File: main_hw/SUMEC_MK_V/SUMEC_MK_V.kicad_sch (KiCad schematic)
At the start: 10 parts

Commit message: 67yfhtgftu
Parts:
- renumbered TP19 to TP1, TP22 to TP10, TP1 to TP2, TP2 to TP3, TP3 to TP4, TP4 to TP5, TP5 to TP6, TP6 to TP7, TP20 to TP8, TP21 to TP9
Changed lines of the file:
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@@
 		(dnp no)
 		(fields_autoplaced yes)
-		(property "Reference" "TP20"
+		(property "Reference" "TP8"
 			(at 165.1 184.6579 0)
 			(effects
@@
 			(project "SUMEC_MK_V"
 				(path "/900bd7ac-cdf9-4a2f-8b1f-2c21e3760046"
-					(reference "TP20")
+					(reference "TP8")
 					(unit 1)
 				)
@@
 		(dnp no)
 		(fields_autoplaced yes)
-		(property "Reference" "TP4"
+		(property "Reference" "TP5"
 			(at 153.67 184.6579 0)
 			(effects
@@
 			(project "SUMEC_MK_V"
 				(path "/900bd7ac-cdf9-4a2f-8b1f-2c21e3760046"
-					(reference "TP4")
+					(reference "TP5")
 					(unit 1)
 				)
@@
 		(dnp no)
 		(fields_autoplaced yes)
-		(property "Reference" "TP3"
+		(property "Reference" "TP4"
 			(at 149.86 184.6579 0)
 			(effects
@@
 			(project "SUMEC_MK_V"
 				(path "/900bd7ac-cdf9-4a2f-8b1f-2c21e3760046"
-					(reference "TP3")
+					(reference "TP4")
 					(unit 1)
 				)
@@
 		(dnp no)
 		(fields_autoplaced yes)
-		(property "Reference" "TP22"
+		(property "Reference" "TP10"
 			(at 172.72 184.6579 0)
 			(effects
@@
 			(project "SUMEC_MK_V"
 				(path "/900bd7ac-cdf9-4a2f-8b1f-2c21e3760046"
-					(reference "TP22")
+					(reference "TP10")
 					(unit 1)
 				)
@@
 		(dnp no)
 		(fields_autoplaced yes)
-		(property "Reference" "TP21"
+		(property "Reference" "TP9"
 			(at 168.91 184.6579 0)
 			(effects
@@
 			(project "SUMEC_MK_V"
 				(path "/900bd7ac-cdf9-4a2f-8b1f-2c21e3760046"
-					(reference "TP21")
+					(reference "TP9")
 					(unit 1)
 				)
@@
 		(dnp no)
 		(fields_autoplaced yes)
-		(property "Reference" "TP5"
+		(property "Reference" "TP6"
 			(at 157.48 184.6579 0)
 			(effects
@@
 			(project "SUMEC_MK_V"
 				(path "/900bd7ac-cdf9-4a2f-8b1f-2c21e3760046"
-					(reference "TP5")
+					(reference "TP6")
 					(unit 1)
 				)
@@
 		(dnp no)
 		(fields_autoplaced yes)
-		(property "Reference" "TP6"
+		(property "Reference" "TP7"
 			(at 161.29 184.6579 0)
 			(effects
@@
 			(project "SUMEC_MK_V"
 				(path "/900bd7ac-cdf9-4a2f-8b1f-2c21e3760046"
-					(reference "TP6")
+					(reference "TP7")
 					(unit 1)
 				)
@@
 		(dnp no)
 		(fields_autoplaced yes)
-		(property "Reference" "TP19"
+		(property "Reference" "TP1"
 			(at 138.43 184.6579 0)
 			(effects
@@
 			(project "SUMEC_MK_V"
 				(path "/900bd7ac-cdf9-4a2f-8b1f-2c21e3760046"
-					(reference "TP19")
+					(reference "TP1")
 					(unit 1)
 				)
@@
 		(dnp no)
 		(fields_autoplaced yes)
-		(property "Reference" "TP1"
+		(property "Reference" "TP2"
 			(at 142.24 184.6579 0)
 			(effects
@@
 			(project "SUMEC_MK_V"
 				(path "/900bd7ac-cdf9-4a2f-8b1f-2c21e3760046"
-					(reference "TP1")
+					(reference "TP2")
 					(unit 1)
 				)
@@
 		(dnp no)
 		(fields_autoplaced yes)
-		(property "Reference" "TP2"
+		(property "Reference" "TP3"
 			(at 146.05 184.6579 0)
 			(effects
@@
 			(project "SUMEC_MK_V"
 				(path "/900bd7ac-cdf9-4a2f-8b1f-2c21e3760046"
-					(reference "TP2")
-					(unit 1)
-				)
+					(reference "TP3")
+					(unit 1)
+				)

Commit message: MK5 changes and deletion of useless files
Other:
- note added: "1. Q: Fix EEPROM 2. Q: I2C expander for more LEDs 3. Q: Power switching for higher voltage (if the battery is connested choose the battery) 4. Q: Fix errors in schematic encoders etc 5. Q: 6. Q: 7. Q:"
- note removed: "*The unit price is set for an order quantity of 10 units"
- note removed: "1. Q: 2. Q: 3. Q: Left/right silk for sensors and motors 4. Q: 5. Q: Add IO pin numbers after the routing is done 6. Q: Does the voltage read need to be after the switch or before? 7. Q:"
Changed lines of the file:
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@@
 		)
 	)
-	(text "1. Q: \n2. Q: \n3. Q: Left/right silk for sensors and motors\n4. Q: \n5. Q: Add IO pin numbers after the routing is done\n6. Q: Does the voltage read need to be after the switch or before?\n7. Q: "
+	(text "1. Q: Fix EEPROM\n2. Q: I2C expander for more LEDs\n3. Q: Power switching for higher voltage \n	(if the battery is connested choose the battery)\n4. Q: Fix errors in schematic encoders etc\n5. Q: \n6. Q: \n7. Q: "
 		(exclude_from_sim no)
 		(at 20.32 183.134 0)
@@
 		)
 	)
-	(text "*The unit price is set for an order quantity of 10 units"
-		(exclude_from_sim no)
-		(at 52.07 173.99 0)
-		(effects
-			(font
-				(face "Bahnschrift")
-				(size 1.905 1.905)
-				(color 255 0 0 1)
-			)
-		)
-	)

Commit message: MK5 PCB rework
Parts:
- removed TP1: TestPoint, sumec_graphic:SUMEC_QR_IMG, symbol Connector:TestPoint
- removed TP10: TestPoint, sumec_graphic:SYMBOL_IMG, symbol Connector:TestPoint
- removed TP2: TestPoint, sumec_graphic:SPS_LOGO_IMG, symbol Connector:TestPoint
- removed TP3: TestPoint, sumec_graphic:SUMEC_LOGO_IMG, symbol Connector:TestPoint
- removed TP4: TestPoint, sumec_graphic:CATTO_MASK_IMG, symbol Connector:TestPoint
- removed TP5: TestPoint, sumec_graphic:OWO_WHATS_THIS_IMG, symbol Connector:TestPoint
- removed TP6: TestPoint, sumec_graphic:HANKA_THINGY_IMG, symbol Connector:TestPoint
- removed TP7: TestPoint, sumec_graphic:CALIPER_IMG, symbol Connector:TestPoint
- removed TP8: TestPoint, sumec_graphic:BEE_IMG, symbol Connector:TestPoint
- removed TP9: TestPoint, sumec_graphic:FLOWER_IMG, symbol Connector:TestPoint
- added BZ1: Buzzer, Schrack_brd:BUZZER_CUI_CPT, symbol Device:Buzzer
- added C1, C11, C16, C17, C20, C22, C23, C24, C25, C26, C4: 100nF, Capacitor_SMD:C_0805_2012Metric_Pad1.18x1.45mm_HandSolder, symbol Device:C
- added C10, C3, C6, C7, C8, C9: 22uF, Capacitor_Tantalum_SMD:CP_EIA-2012-12_Kemet-R_Pad1.30x1.05mm_HandSolder, symbol Device:C_Polarized
- added C12, C14: 22nF, Capacitor_SMD:C_0805_2012Metric_Pad1.18x1.45mm_HandSolder, symbol Device:C_Small
- added C13, C15, C5: 100nF, Capacitor_SMD:C_0805_2012Metric_Pad1.18x1.45mm_HandSolder, symbol Device:C_Small
- added C18, C19, C2, C21: 10uF, Capacitor_Tantalum_SMD:CP_EIA-3216-18_Kemet-A_Pad1.58x1.35mm_HandSolder, symbol Device:C_Polarized
- added C27, C29: 10uF, Capacitor_Tantalum_SMD:CP_EIA-3216-18_Kemet-A_Pad1.58x1.35mm_HandSolder, symbol Device:C_Polarized_Small
- added C28, C33, C34, C35, C36, C37: 100n, Capacitor_SMD:C_0805_2012Metric, symbol Device:C_Small
- added C30: 1u, Capacitor_SMD:C_0805_2012Metric, symbol Device:C_Small
- added C31, C32: 18p, Capacitor_SMD:C_0805_2012Metric, symbol Device:C_Small
- added D1, D2: D_Schottky, Diode_SMD:D_1206_3216Metric_Pad1.42x1.75mm_HandSolder, symbol Device:D_Schottky
- added D10: ALRT2, LED_SMD:LED_0805_2012Metric, symbol Device:LED_Small
- added D11, D12: D_Schottky, Diode_SMD:D_1206_3216Metric, symbol Device:D_Schottky
- added D3: D, symbol Device:D
- added D4, D5, D6, D7, D8, D9: LED, LED_SMD:LED_0805_2012Metric_Pad1.15x1.40mm_HandSolder, symbol Device:LED
- added H1, H2: Mounting Hole M3, MountingHole:MountingHole_3.2mm_M3_Pad_Via, symbol Mechanical:MountingHole_Pad
- added IC1: TPS565242DRLR, Package_TO_SOT_SMD:SOT-563, symbol SamacSys_Parts:TPS565242DRLR
- added IC2, IC3: DRV8874PWPR, sumec_brd:DRV8874, symbol sumec_sch_lib:DRV8874PWPR
- added J1: XT30PW-M, sumec_brd:XT30PW-M, symbol sumec_sch_lib:XT30PW-M
- added J10, J12, J13, J7, J8, J9: Conn_01x03_Pin, Connector_Molex:Molex_PicoBlade_53398-0371_1x03-1MP_P1.25mm_Vertical, symbol Connector:Conn_01x03_Pin
- added J11: Conn_01x03_Pin, Connector_PinHeader_2.54mm:PinHeader_1x03_P2.54mm_Vertical, symbol Connector:Conn_01x03_Pin
- added J14, J15, J4: USB_TypeC, sumec_brd:HRO_TYPE-C-31-M-12, symbol sumec_sch_lib:USB_TypeC
- added J2, J3: Conn_01x06_Socket, Connector_JST:JST_SH_BM06B-SRSS-TB_1x06-1MP_P1.00mm_Vertical, symbol Connector:Conn_01x06_Socket
- added J5: Conn_01x04_Pin, Connector_Molex:Molex_PicoBlade_53398-0471_1x04-1MP_P1.25mm_Vertical, symbol Connector:Conn_01x04_Pin
- added J6: Conn_01x06_Pin, Connector_Molex:Molex_PicoBlade_53398-0671_1x06-1MP_P1.25mm_Vertical, symbol Connector:Conn_01x06_Pin
- added JP1, JP2, JP3: SolderJumper_3_Open, Jumper:SolderJumper-3_P2.0mm_Open_TrianglePad1.0x1.5mm, symbol Jumper:SolderJumper_3_Open
- added JP4, JP5, JP6: Jumper_2_Small_Open, Jumper:SolderJumper-2_P1.3mm_Open_RoundedPad1.0x1.5mm, symbol Jumper:Jumper_2_Small_Open
- added L1: 1.5uH, Inductor_SMD:L_Vishay_IHLP-1212, symbol Device:L
- added L2: 3.3uH, Inductor_SMD:L_Vishay_IHLP-1616, symbol Device:L
- added Q1: Q_PMOS, Package_TO_SOT_SMD:SOT-23-3, symbol Device:Q_PMOS_GSD
- added Q2: SI2393DS, Package_TO_SOT_SMD:SOT-23-3, symbol Device:Q_PMOS_GSD
- added R1: 2m, Resistor_SMD:R_0805_2012Metric_Pad1.20x1.40mm_HandSolder, symbol Device:R
- added R10, R25, R26, R9: 10k, Resistor_SMD:R_0805_2012Metric_Pad1.20x1.40mm_HandSolder, symbol Device:R_Small
- added R11, R12, R2, R23, R24, R27, R3, R7: 10k, Resistor_SMD:R_0805_2012Metric_Pad1.20x1.40mm_HandSolder, symbol Device:R
- added R13: 1k, Resistor_SMD:R_0805_2012Metric_Pad1.20x1.40mm_HandSolder, symbol Device:R
- added R14, R16, R17, R20, R21: 220R, Resistor_SMD:R_0805_2012Metric_Pad1.20x1.40mm_HandSolder, symbol Device:R
- added R15: 100k, Resistor_SMD:R_0805_2012Metric_Pad1.20x1.40mm_HandSolder, symbol Device:R
- added R18, R19: 15R, Resistor_SMD:R_0805_2012Metric_Pad1.20x1.40mm_HandSolder, symbol Device:R
- added R22: 0R, Resistor_SMD:R_0805_2012Metric_Pad1.20x1.40mm_HandSolder, symbol Device:R
- added R28: 100R, Resistor_SMD:R_0805_2012Metric_Pad1.20x1.40mm_HandSolder, symbol Device:R
- added R29, R30, R31, R32, R33, R38: 10k, Resistor_SMD:R_0805_2012Metric, symbol Device:R_Small
- added R34, R40: 100k, Resistor_SMD:R_0805_2012Metric, symbol Device:R_Small
- added R35, R36: 15R, Resistor_SMD:R_0805_2012Metric, symbol Device:R
- added R37: 50m, Resistor_SMD:R_0805_2012Metric, symbol Device:R
- added R39: 2.2k, Resistor_SMD:R_0805_2012Metric, symbol Device:R_Small
- added R4: 45k, Resistor_SMD:R_0805_2012Metric_Pad1.20x1.40mm_HandSolder, symbol Device:R
- added R41, R42: 5.1k, Resistor_SMD:R_0805_2012Metric, symbol Device:R_Small
- added R43, R44: 15R, Resistor_SMD:R_0805_2012Metric, symbol Device:R_Small
- added R45: 10k, Resistor_SMD:R_0805_2012Metric, symbol Device:R
- added R5: 100k, Resistor_SMD:R_0805_2012Metric_Pad1.20x1.40mm_HandSolder, symbol Device:R_Small
- added R6, R8: 52.3k, Resistor_SMD:R_0805_2012Metric_Pad1.20x1.40mm_HandSolder, symbol Device:R_Small
- added SW1: SW_DPDT_x2, sumec_brd:Custom_SPDT_2.5_Switch, symbol Switch:SW_DPDT_x2
- added SW2, SW3, SW4, SW5: SW_Push, sumec_brd:SW_SPST_EVQPE1, symbol Switch:SW_Push
- added SW6: RST, gps-compass_brd:SW_SPST_EVQPE1, symbol Switch:SW_Push
- added TP11, TP12, TP13, TP14, TP15, TP16, TP17, TP18, TP19, TP20, TP21, TP22, TP23, TP24, TP25: TestPoint, TestPoint:TestPoint_Pad_D1.0mm, symbol Connector:TestPoint
- added U1, U8: INA226, Package_SO:VSSOP-10_3x3mm_P0.5mm, symbol Sensor_Energy:INA226
- added U2: AP62300Z6, Package_TO_SOT_SMD:SOT-563, symbol Regulator_Switching:AP62300Z6
- added U3: 24CW1280T-I/OT, Package_TO_SOT_SMD:SOT-23-5, symbol Memory_EEPROM:24AA02-OT
- added U4: ESP32-S3-WROOM-1, PCM_Espressif:ESP32-S3-WROOM-1, symbol sumec_sch_lib:ESP32-S3-WROOM-1_CUSTOM_made_by_bismarx
- added U5, U7, U9: USBLC6-2SC6, Package_TO_SOT_SMD:TSOT-23-6_HandSoldering, symbol sumec_library:USBLC6-2SC6
- added U6: BNO055, Package_LGA:LGA-28_5.2x3.8mm_P0.5mm, symbol Sensor_Motion:BNO055
- added Y1: 32.768k, gps-compass_brd:CM8V32768TA020125, symbol Device:Crystal
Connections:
- new net: D9.2 (A), R21.2
- new net: R5.2, R6.1, U2.5 (EN)
- new net: C15.1, IC3.12 (VCP)
- new net: D8.2 (A), R20.2
- new net: C33.1, J14.S1 (SHIELD), J14.S2 (SHIELD), J14.S3 (SHIELD), J14.S4 (SHIELD), R34.1
- new net: D4.2 (A), R13.2
- new net: C12.1, IC2.14 (CPL)
- new net: C12.2, IC2.13 (CPH)
- new net: D5.2 (A), R14.2
- new net: C32.1, U6.27 (XIN32), Y1.1
- new net: C31.1, U6.26 (XOUT32), Y1.2
- new net: JP5.1 (A), R32.2, U6.6 (PS0)
- new net: R30.1, SW6.2, U6.11 (~{RESET})
- new net: JP4.1 (A), R31.2, U6.17 (COM3)
- new net: R29.1, TP25.1, U6.4 (~{BOOT_LOAD_PIN})
- new net: JP6.1 (A), R33.2, U6.5 (PS1)
- new net: C30.1, U6.9 (CAP)
- new net: R43.2, U9.1
- new net: R44.2, U9.3
- new net: D10.1 (K), R38.2, U8.3 (~{Alert})
- new net: C34.1, U7.5
- new net: C13.1, IC2.12 (VCP)
- new net: D6.2 (A), R16.2
- new net: J15.A5 (CC1), R42.1
- new net: J15.B5 (CC2), R41.2
- new net: C36.2, J15.S1 (SHIELD), J15.S2 (SHIELD), J15.S3 (SHIELD), J15.S4 (SHIELD), R40.2
- new net: R18.2, U5.1
- new net: D10.2 (A), R39.2
- new net: R19.2, U5.3
- new net: C14.2, IC3.13 (CPH)
- new net: C14.1, IC3.14 (CPL)
- new net: C5.2, U2.4 (BST)
- new net: J7.2 (Pin_2), R28.2
- new net: D11.2 (A), Q2.3 (D)
- new net: IC1.2 (SW), L1.1
- new net: R36.2, U7.3
- new net: BZ1.1 (+), R22.2
- new net: R35.2, U7.1
- new net: D7.2 (A), R17.2
- new net +12V: C13.2, C15.2, C16.2, C17.2, C18.1, C19.1, C2.1, IC2.11 (VM), IC3.11 (VM), Q1.3 (D), R13.1, R5.1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
- new net +3V3: C1.2, C11.1, C20.1, C21.1, C22.1, C27.1, C28.1, C29.1, C35.1, C6.1, C7.1, C9.1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
- new net +5V: C3.1, C4.1, D1.1 (K), D3.1 (K), IC1.1 (VIN), IC1.5 (EN), J6.1 (Pin_1), TP12.1
- new net ACC_INT: U4.32 (IO39)
- new net BOOT: C26.1, R24.1, SW3.2, U4.27 (IO0)
- new net BTN_IO04: R25.2, SW4.2, U4.4 (IO4)
- new net BTN_IO05: R26.2, SW5.2, U4.5 (IO5)
- new net BZ_IO02: R22.1, U4.38 (IO2)
- new net CC1: J14.A5 (CC1)
- new net CC2: J14.B5 (CC2)
- new net D+: U4.14 (IO20), U5.4, U7.4, U9.6
- new net D-: U4.13 (IO19), U5.6, U7.6, U9.4
- new net DN_IN: J14.A7 (DN1), J14.B7 (DN2), J15.A7 (DN1), J15.B7 (DN2), R35.1, R44.1
- new net DP_IN: J14.A6 (DP1), J14.B6 (DP2), J15.A6 (DP1), J15.B6 (DP2), R36.1, R43.1
- new net D_NEG_IN: J4.A7 (DN1), J4.B7 (DN2), R18.1
- new net D_POS_IN: J4.A6 (DP1), J4.B6 (DP2), R19.1
- new net EN: C25.1, R23.1, SW2.2, U4.3 (EN)
- new net EN_L: IC2.1 (EN/IN1), TP15.1, U4.7 (IO7)
- new net EN_R: IC3.1 (EN/IN1), TP18.1, U4.12 (IO8)
- new net FB: IC1.6 (FB), R4.2, R7.1
- new net FB_5V: R8.2, R9.1, U2.6 (FB)
- new net FET_SW: Q1.1 (G), R2.2, SW1.1 (A)
- new net GND: BZ1.2 (-), C1.1, C10.2, C11.2, C16.1, C17.1, C18.2, C19.2, C2.2, C20.2, C21.2, C22.2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
- new net GYR_INT: U4.33 (IO40)
- new net INT_IMU: U6.14 (INT)
- new net IN_NEG_2: R37.2, U8.8 (Vbus), U8.9 (Vin-)
- new net IR_MODULE: J11.1 (Pin_1), TP19.1, U4.30 (IO37)
- new net LED_IO01: R21.1, U4.39 (IO1)
- new net LED_IO36: R20.1, U4.29 (IO36)
- new net LED_IO43: U4.37 (IO43)
- new net LED_IO44: R16.1, U4.36 (IO44)
- new net LED_IO47: R17.1
- new net MOTOR_L_1: IC2.8 (OUT1), J2.6 (Pin_6), TP23.1
- new net MOTOR_L_2: IC2.10 (OUT2), J2.5 (Pin_5), TP24.1
- new net MOTOR_R_1: IC3.8 (OUT1), J3.6 (Pin_6), TP21.1
- new net MOTOR_R_2: IC3.10 (OUT2), J3.5 (Pin_5), TP22.1
- new net OUT_L_A: J2.3 (Pin_3)
- new net OUT_L_B: J2.2 (Pin_2)
- new net OUT_R_A: J3.3 (Pin_3)
- new net OUT_R_B: J3.2 (Pin_2)
- new net PH_L: IC2.2 (PH/IN2), TP17.1, U4.6 (IO6)
- new net PH_R: IC3.2 (PH/IN2), TP20.1, U4.11 (IO18)
- new net PMODE_1: IC2.16 (PMODE), JP2.2 (C)
- new net PMODE_2: IC3.16 (PMODE), JP3.2 (C)
- new net POL_L: J10.1 (Pin_1), U4.28 (IO35)
- new net POL_M: J9.1 (Pin_1), U4.19 (IO11)
- new net POL_R: J8.1 (Pin_1), U4.20 (IO12)
- new net QRE_BACK: J7.1 (Pin_1), R27.2, U4.9 (IO16)
- new net QRE_L: J5.4 (Pin_4), U4.22 (IO14)
- new net QRE_R: J5.1 (Pin_1), U4.21 (IO13)
- new net SCL: J6.3 (Pin_3), R12.1, U1.5 (SCL), U3.1 (SCL), U4.34 (IO41), U6.19 (COM1), U8.5 (SCL)
- new net SDA: J6.2 (Pin_2), R11.1, U1.4 (SDA), U3.3 (SDA), U4.35 (IO42), U6.20 (COM0), U8.4 (SDA)
- new net SHARP_L: J13.1 (Pin_1), U4.31 (IO38)
- new net SHARP_R: J12.1 (Pin_1), U4.18 (IO10)
- new net SHLD: C23.2, J4.S1 (SHIELD), J4.S2 (SHIELD), J4.S3 (SHIELD), J4.S4 (SHIELD), R15.1
- new net SW: C5.1, L2.1, U2.2 (SW)
- new net USB_VBUS: C24.1, C37.2, D12.2 (A), J14.A4_B9 (VBUS), J14.B4_A9 (VBUS), J15.A4_B9 (VBUS), J15.B4_A9 (VBUS), J4.A4_B9 (VBUS), J4.B4_A9 (VBUS), Q2.1 (G), R45.1, U5.5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
- new net VBATT: J1.P, JP1.3 (B), R1.1, U1.10 (Vin+)
- new net VBATT_SHUNT: JP1.1 (A), Q1.2 (S), R1.2, R2.1, U1.9 (Vin-)
- new net VBATT_SW: Q2.2 (S)
- new net VBUS_INA226: JP1.2 (C), U1.8 (Vbus)
- new net VBUS_USB: D3.2 (A), R14.1, TP13.1
- new net VIN: D11.1 (K), D12.1 (K)
- new net VOLTAGE_ALERT: R3.2, U1.3 (~{Alert}), U4.17 (IO9)
- new net VOUT_5V: C10.1, C8.1, D1.2 (A), L2.2, R8.1
- new net nFAULT: IC2.4 (NFAULT), IC3.4 (NFAULT), R10.1, TP11.1
- no-connect marks 0 -> 16
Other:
- removed sheet CONNECTIVITY
- removed sheet MCU
- removed sheet MECHANICS
- removed sheet MOTOR CONTROL
- removed sheet POWER
- removed sheet SENSORICS
- note added: "( Better manual in -DOCS- )"
- note added: "- 2S/3S LiPo - 3.7V Cell voltage (nominal voltage) - 4,2V Cell voltage (fully charged) - 400mAh (may vary)"
- note added: "1. 2. 3. 4. 5. 6. 7."
- note added: "6-PIN JST SH-Style male connector VCC 2.7 V to 18 V encoder operating voltage"
- note added: "9-AXIS IMU"
- note added: "AP62301Z6-7 Step down converter Input: 4.2-18V Output: 5V Current output: 3A Switching freq.: 750kHz Inductor Inductance: 3.3uH Max. current: 2.7A"
- note added: "BAD PINOUT"
- note added: "BATTERY"
- note added: "BNO055 9 DOF Absolute IMU with intergrated sensor fusion"
- note added: "BOOT"
- note added: "BUZZER"
- note added: "Battery power"
- note added: "Buttons for BOOT and ENABLE functions. If the device does not support the auto download mode, you need to get into the download mode manually. To do so, press and hold the BOOT button and then press the RESET button once. After that release the BOOT button."
- note added: "CONNECTORS and MISC"
- note added: "CONTROL MODES: PMODE HIGH = PWM PMODE LOW = PH/EN"
- note added: "CURRENT READING - 2"
- note added: "DEBUG and MECHANICS"
- note added: "DISTANCE MEASURING"
- note added: "DRV8874 - Motor driver, H-Bridge Recommended Operating Conditions VM = 4.5V - 37V VM VIN = 0V - 5v I/PMODE, nSlEEP, EN/IN1, PH/IN2 fPWM = 0Hz - 100kHz EN/IN1, PH/IN2 Vref = 0V - 3.6V VREF Block Diagram:"
- note added: "Default Configuration of Strapping Pins Strapping Pin Default Configuration Bit Value GPIO0 Pull-up 1 GPIO3 Floating - GPIO45 Pull-down 0 GPIO46 Pull-down 0"
- note added: "Digital distance sensor - Sharp GP2Y0D810Z0F Sensor detects objects between 2 cm and 10 cm Low when detecting an object, high otherwise. Operating voltage 2.7V - 6.2V"
- note added: "EEPROM"
- note added: "EN-IN1"
- note added: "EN=reset, BOOT=bootloader mode Enable (EN) is the 3.3V regulator's enable pin. It's pulled up, so connect to ground to disable the 3.3V regulator. This means that you can use this pin connected to a pushbutton to restart your ESP32, for example."
- note added: "ENABLE RESET"
- note added: "ESD PROTECTION"
- note added: "ESP32-S3 Datasheet"
- note added: "ESP32-S3-WROOM1-N4"
- note added: "GPIO USB 20 D+ (green) 19 D- (white) GND GND (black) VBUS +5V (red)"
- note added: "GPIO0 has an internal pullup resistor, so if it is left unconnected then it will pull high."
- note added: "GPIO0, GPIO45, and GPIO46 are connected to the chip's internal weak pull-up/pull-down resistors at chip reset. These resistors determine the default bit values of the strapping pins. Also, these resistors determine the bit values if the strapping pins are connected to an external high-impedance circuit."
- note added: "H-BRIDGE"
- note added: "I2C Addr.: 0x28"
- note added: "I2C Addr.: 0x50"
- note added: "I2C adress = 0x40"
- note added: "I2C adress = 0x44, 1000100"
- note added: "IR LED Reciver module Operating voltage: 2.7V to 5.5V Frequency: 38kHz"
- note added: "IR MODULE"
- note added: "ITRIP (A) x AIPROPI (μA/A) = VVREF (V) / RIPROPI (Ω)"
- note added: "LED SIGNALISATION"
- note added: "LEFT"
- note added: "LINE SENSORS"
- note added: "M3 Padded Mounting holes"
- note added: "MAIN SWITCH"
- note added: "MCU and IMU"
- note added: "MIRRORED"
- note added: "MOTOR - LEFT"
- note added: "MOTOR - RIGHT"
- note added: "MOTORS"
- note added: "MOUNTING"
- note added: "Memory: 128kbit Ma freq.: 1MHz Vin: 1.6-5.5V Access time: 450ns Max supply curr.: 1mA"
- note added: "Miniature Reflective Object Sensor - QRE1113"
- note added: "NAME | GPIO | DESC. BOOT | 00 | BOOT mode, button LED_IO01 | 01 | LED, Indication, --debug BZ_IO02 | 02 | Buzzer, Indication --debug STRAP | 03 | STRAPPING PIN, DO NOT CONNECT BTN_IO04 | 04 | Button, INPUT_PULLPIT needed BTN_IO05 | 05 | Button, INPUT_PULLPIT needed PH_L | 06 | EN_L | 07 | EN_R | 08 | cSelect0 | 09 | cSelect1 | 10 | D_EXT1 | 11 | D_EXT2 | 12 | D_EXT3 | 13 | MODE_SW | 14 | RESET_SW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"
- note added: "NO POL_L CONNECTED FIX TO IO35 NO ENCODERS CONNECTED FIX TO 4 AVAILABLE PINS"
- note added: "OBJECT DETECTING SENSORS"
- note added: "PH-IN2"
- note added: "POLOLU SENSOR MANUAL"
- note added: "POWER MANAGMENT and SOURCES"
- note added: "PUSH BUTTONS"
- note added: "Pololu Distance Sensor with Pulse Width Output/Digital Output Small lidar based sensor can report presnece/distance of objects up to (TOTAL MAX 200cm-Digital, 300cm - PWM) Distance is chosen by configurating the jumpers with 0R resistors"
- note added: "Power switching between 5V VBUS - USB and 5V Buck converter - BATT"
- note added: "RIGHT"
- note added: "Rds On = 22.7 mOhms Vds = 30 V Vgs = - 20 V, + 16 V Vgs th = 2.2 V"
- note added: "SIDE SENSORS"
- note added: "SOME PINS ARE NOT CONNECTED IN SCHEMATIC"
- note added: "STEPDOWN CONVERTER 3.3V"
- note added: "STEPDOWN CONVERTER 5V"
- note added: "SWITCHING SIMULATION - FALSTAD"
- note added: "Status LED1"
- note added: "Status LED2"
- note added: "Status LED3"
- note added: "Status LED4"
- note added: "TESTING POINTS"
- note added: "TF-LUNA MANUAL"
- note added: "TO-DO LIST"
- note added: "TPS62133 Step down converter Input: 3-17V Output: 5V Current output: 3A Switching freq.: 2.5MHz Inductor Inductance: 2.2uH Max. current: 4.7A"
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
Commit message: MK5 new update of the PCB
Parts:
- removed C1, C11, C16, C17, C20, C22, C23, C24, C25, C26, C4: 100nF, Capacitor_SMD:C_0805_2012Metric_Pad1.18x1.45mm_HandSolder, symbol Device:C
- removed C10, C3, C6, C7, C8, C9: 22uF, Capacitor_Tantalum_SMD:CP_EIA-2012-12_Kemet-R_Pad1.30x1.05mm_HandSolder, symbol Device:C_Polarized
- removed C18, C19, C2, C21: 10uF, Capacitor_Tantalum_SMD:CP_EIA-3216-18_Kemet-A_Pad1.58x1.35mm_HandSolder, symbol Device:C_Polarized
- removed C27, C29: 10uF, Capacitor_Tantalum_SMD:CP_EIA-3216-18_Kemet-A_Pad1.58x1.35mm_HandSolder, symbol Device:C_Polarized_Small
- removed C33, C34, C35: 100n, Capacitor_SMD:C_0805_2012Metric, symbol Device:C_Small
- removed D1, D2: D_Schottky, Diode_SMD:D_1206_3216Metric_Pad1.42x1.75mm_HandSolder, symbol Device:D_Schottky
- removed D10: ALRT2, LED_SMD:LED_0805_2012Metric, symbol Device:LED_Small
- removed D3: D, symbol Device:D
- removed D7: LED, LED_SMD:LED_0805_2012Metric_Pad1.15x1.40mm_HandSolder, symbol Device:LED
- removed IC1: TPS565242DRLR, Package_TO_SOT_SMD:SOT-563, symbol SamacSys_Parts:TPS565242DRLR
- removed J14, J15, J4: USB_TypeC, sumec_brd:HRO_TYPE-C-31-M-12, symbol sumec_sch_lib:USB_TypeC
- removed JP1, JP2, JP3: SolderJumper_3_Open, Jumper:SolderJumper-3_P2.0mm_Open_TrianglePad1.0x1.5mm, symbol Jumper:SolderJumper_3_Open
- removed Q2: SI2393DS, Package_TO_SOT_SMD:SOT-23-3, symbol Device:Q_PMOS_GSD
- removed R1: 2m, Resistor_SMD:R_0805_2012Metric_Pad1.20x1.40mm_HandSolder, symbol Device:R
- removed R11, R12, R2, R23, R24, R3, R7: 10k, Resistor_SMD:R_0805_2012Metric_Pad1.20x1.40mm_HandSolder, symbol Device:R
- removed R15: 100k, Resistor_SMD:R_0805_2012Metric_Pad1.20x1.40mm_HandSolder, symbol Device:R
- removed R16, R17, R20, R21: 220R, Resistor_SMD:R_0805_2012Metric_Pad1.20x1.40mm_HandSolder, symbol Device:R
- removed R18, R19: 15R, Resistor_SMD:R_0805_2012Metric_Pad1.20x1.40mm_HandSolder, symbol Device:R
- removed R22: 0R, Resistor_SMD:R_0805_2012Metric_Pad1.20x1.40mm_HandSolder, symbol Device:R
- removed R25, R26: 10k, Resistor_SMD:R_0805_2012Metric_Pad1.20x1.40mm_HandSolder, symbol Device:R_Small
- removed R28: 100R, Resistor_SMD:R_0805_2012Metric_Pad1.20x1.40mm_HandSolder, symbol Device:R
- removed R34: 100k, Resistor_SMD:R_0805_2012Metric, symbol Device:R_Small
- removed R36: 15R, Resistor_SMD:R_0805_2012Metric, symbol Device:R
- removed R38: 10k, Resistor_SMD:R_0805_2012Metric, symbol Device:R_Small
- removed R39: 2.2k, Resistor_SMD:R_0805_2012Metric, symbol Device:R_Small
- removed R4: 45k, Resistor_SMD:R_0805_2012Metric_Pad1.20x1.40mm_HandSolder, symbol Device:R
- removed R45: 10k, Resistor_SMD:R_0805_2012Metric, symbol Device:R
- removed SW2: SW_Push, sumec_brd:SW_SPST_EVQPE1, symbol Switch:SW_Push
- removed TP15, TP17, TP18, TP19, TP20, TP21, TP22, TP23, TP24: TestPoint, TestPoint:TestPoint_Pad_D1.0mm, symbol Connector:TestPoint
- removed U3: 24CW1280T-I/OT, Package_TO_SOT_SMD:SOT-23-5, symbol Memory_EEPROM:24AA02-OT
- removed U4: ESP32-S3-WROOM-1, PCM_Espressif:ESP32-S3-WROOM-1, symbol sumec_sch_lib:ESP32-S3-WROOM-1_CUSTOM_made_by_bismarx
- removed U5, U7: USBLC6-2SC6, Package_TO_SOT_SMD:TSOT-23-6_HandSoldering, symbol sumec_library:USBLC6-2SC6
- removed U8: INA226, Package_SO:VSSOP-10_3x3mm_P0.5mm, symbol Sensor_Energy:INA226
- added C1, C15, C18, C30, C31, C6, C7: 100n, Capacitor_SMD:C_0805_2012Metric, symbol Device:C_Small
- added C10, C11, C12, C14, C29, C9: 10u, Capacitor_SMD:C_0805_2012Metric, symbol Device:C_Small
- added C16, C17, C19, C20, C22, C23: 22u, Capacitor_SMD:C_0805_2012Metric, symbol Device:C_Small
- added C28: 100n, Capacitor_SMD:C_0805_2012Metric, symbol Device:C
- added D10, D11, D5: LED, LED_SMD:LED_0805_2012Metric, symbol Device:LED
- added D3: LED, LED_SMD:LED_0805_2012Metric, symbol Device:LED_Small
- added J4: USB_C, sumec_brd:USB_C_Receptacle_GCT_USB4105-xx-A_16P_TopMnt_Horizontal, symbol Connector:USB_C_Receptacle_USB2.0_16P
- added JP1, JP2: Jumper_2_Small_Open, Jumper:SolderJumper-2_P1.3mm_Open_RoundedPad1.0x1.5mm, symbol Jumper:Jumper_2_Small_Open
- added R1: 2m, Resistor_SMD:R_0805_2012Metric, symbol Device:R_Small
- added R13: 45k, Resistor_SMD:R_0805_2012Metric, symbol Device:R_Small
- added R14, R17, R29, R3, R30, R36, R40, R5, R7, R8: 10k, Resistor_SMD:R_0805_2012Metric, symbol Device:R_Small
- added R18: 100R, Resistor_SMD:R_0805_2012Metric, symbol Device:R_Small
- added R26: 10k, Resistor_SMD:R_0805_2012Metric, symbol Device:R
- added R28: 0R, Resistor_SMD:R_0805_2012Metric, symbol Device:R_Small
- added R32, R33, R38, R39: 220R, Resistor_SMD:R_0805_2012Metric, symbol Device:R
- added R4: 2.2k, Resistor_SMD:R_0805_2012Metric, symbol Device:R_Small
- added SW6: BOOT, gps-compass_brd:SW_SPST_EVQPE1, symbol Switch:SW_Push
- added TP10, TP12, TP3, TP5, TP7, TP8, TP9: TestPoint, TestPoint:TestPoint_Pad_D1.5mm, symbol Connector:TestPoint
- added U5: TPS565242DRLR, Package_TO_SOT_SMD:SOT-563, symbol SamacSys_Parts:TPS565242DRLR
- added U8: ESP32-S3-WROOM-1, PCM_Espressif:ESP32-S3-WROOM-1, symbol sumec_sch_lib:ESP32-S3-WROOM-1_CUSTOM_made_by_bismarx
- added U9: 24CW1280T-I/OT, Package_TO_SOT_SMD:SOT-23-5, symbol Memory_EEPROM:24AA02-OT
- C13: renamed from C5; value 100nF -> 100n; footprint Capacitor_SMD:C_0805_2012Metric_Pad1.18x1.45mm_HandSolder -> Capacitor_SMD:C_0805_2012Metric
- C2: renamed from C12; value 22nF -> 22n; footprint Capacitor_SMD:C_0805_2012Metric_Pad1.18x1.45mm_HandSolder -> Capacitor_SMD:C_0805_2012Metric
- C3: renamed from C13; value 100nF -> 100n; footprint Capacitor_SMD:C_0805_2012Metric_Pad1.18x1.45mm_HandSolder -> Capacitor_SMD:C_0805_2012Metric
- C4: renamed from C14; value 22nF -> 22n; footprint Capacitor_SMD:C_0805_2012Metric_Pad1.18x1.45mm_HandSolder -> Capacitor_SMD:C_0805_2012Metric
- C5: renamed from C15; value 100nF -> 100n; footprint Capacitor_SMD:C_0805_2012Metric_Pad1.18x1.45mm_HandSolder -> Capacitor_SMD:C_0805_2012Metric
- D4, D6, D8, D9: footprint LED_SMD:LED_0805_2012Metric_Pad1.15x1.40mm_HandSolder -> LED_SMD:LED_0805_2012Metric
- D7: renamed from D5; footprint LED_SMD:LED_0805_2012Metric_Pad1.15x1.40mm_HandSolder -> LED_SMD:LED_0805_2012Metric
- J13: renamed from J11; footprint Connector_PinHeader_2.54mm:PinHeader_1x03_P2.54mm_Vertical -> TerminalBlock_Phoenix:TerminalBlock_Phoenix_MPT-0,5-3-2.54_1x03_P2.54mm_Horizontal
- L2: renamed from L1; value 1.5uH -> 2.2u
- Q1: value Q_PMOS -> PMOS
- R11: renamed from R5; footprint Resistor_SMD:R_0805_2012Metric_Pad1.20x1.40mm_HandSolder -> Resistor_SMD:R_0805_2012Metric
- R12: renamed from R6; footprint Resistor_SMD:R_0805_2012Metric_Pad1.20x1.40mm_HandSolder -> Resistor_SMD:R_0805_2012Metric
- R19: renamed from R8; footprint Resistor_SMD:R_0805_2012Metric_Pad1.20x1.40mm_HandSolder -> Resistor_SMD:R_0805_2012Metric
- R2: renamed from R10; footprint Resistor_SMD:R_0805_2012Metric_Pad1.20x1.40mm_HandSolder -> Resistor_SMD:R_0805_2012Metric
- R20: renamed from R9; footprint Resistor_SMD:R_0805_2012Metric_Pad1.20x1.40mm_HandSolder -> Resistor_SMD:R_0805_2012Metric
- R27: footprint Resistor_SMD:R_0805_2012Metric_Pad1.20x1.40mm_HandSolder -> Resistor_SMD:R_0805_2012Metric
- R31: renamed from R13; value 1k -> 2.2k; footprint Resistor_SMD:R_0805_2012Metric_Pad1.20x1.40mm_HandSolder -> Resistor_SMD:R_0805_2012Metric
- R34: renamed from R14; footprint Resistor_SMD:R_0805_2012Metric_Pad1.20x1.40mm_HandSolder -> Resistor_SMD:R_0805_2012Metric
- R35: value 15R -> 220R
- R37: value 50m -> 220R
- SW3: value SW_Push -> RESET; footprint sumec_brd:SW_SPST_EVQPE1 -> gps-compass_brd:SW_SPST_EVQPE1
- SW4, SW5: value SW_Push -> BOOT; footprint sumec_brd:SW_SPST_EVQPE1 -> gps-compass_brd:SW_SPST_EVQPE1
- TP1: renamed from TP25; footprint TestPoint:TestPoint_Pad_D1.0mm -> TestPoint:TestPoint_Pad_D1.5mm
- TP11, TP13: footprint TestPoint:TestPoint_Pad_D1.0mm -> TestPoint:TestPoint_Pad_D1.5mm
- TP2: renamed from TP12; footprint TestPoint:TestPoint_Pad_D1.0mm -> TestPoint:TestPoint_Pad_D1.5mm
- TP4: renamed from TP14; footprint TestPoint:TestPoint_Pad_D1.0mm -> TestPoint:TestPoint_Pad_D1.5mm
- TP6: renamed from TP16; footprint TestPoint:TestPoint_Pad_D1.0mm -> TestPoint:TestPoint_Pad_D1.5mm
- U6: renamed from U9; footprint Package_TO_SOT_SMD:TSOT-23-6_HandSoldering -> Package_TO_SOT_SMD:TSOT-23-6; DESCRIPTION 17V Clamp 5A (8/20µs) Ipp Tvs Diode Surface Mount SOT-23-6 -> (none)
- renumbered C37 to C21, C28 to C24, C30 to C25, C31 to C26, C32 to C27, C36 to C8, D11 to D1, D12 to D2, J9 to J10, J10 to J11, J6 to J12, J12 to J5, J5 to J6, J13 to J8, J8 to J9, JP4 to JP3, JP5 to JP4, JP6 to JP5, L2 to L1, R41 to R10, R44 to R15, R43 to R16, R29 to R21, R30 to R22, R31 to R23, R32 to R24, R33 to R25, R40 to R6, R42 to R9, SW6 to SW2, IC2 to U2, IC3 to U3, U2 to U4, U6 to U7
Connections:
- net BTN_IO04 is gone; now on net BOOT: SW4.2
- net IN_NEG_2 is gone; now on net GND: R37.2
- net IR_MODULE is gone; now on net +3V3: J13.1 (Pin_1)
- net VBUS_INA226 is gone; now on net VSHUNT: U1.8 (Vbus)
- net VIN is gone; now on net +5V: D1.1 (K), D2.1 (K)
- net VOUT_5V is gone; now on net VOUT: L1.2, R19.1
- net +12V: now also TP2.1, C10.1, C11.1, C6.1, C7.1, C9.1; no longer TP6.1
- net +3V3: now also R27.2, TP6.1, C1.2, C12.1, C14.1, C18.1, C19.1, C22.1, C23.1, C29.1, C30.1, C31.2, JP1.2 (B), JP2.2 (B), R13.2, R17.2, R18.1, R26.2, R29.2, R3.2, R30.2, R33.1, R36.2, R4.1, R40.2, U8.2 (3V3), U9.4 (V_{CC}); no longer J13.3 (Pin_3), R27.1, R37.1, TP4.1
- net +5V: now also TP4.1, C15.1, C16.1, R32.1, U5.1 (VIN), U5.5 (EN); no longer TP2.1
- net BOOT: now also R27.1, U8.27 (IO0); no longer SW3.2
- net D+: now also U6.4, U8.14 (IO20); no longer U6.6
- net D-: now also U6.6, U8.13 (IO19); no longer U6.4
- net DN_IN: now also J4.A7 (D-), J4.B7 (D-); no longer R35.1
- net DP_IN: now also J4.A6 (D+), J4.B6 (D+)
- net EN: now also SW3.2, C28.2, R26.1, U8.3 (EN)
- net EN_L: now also U8.10 (IO17)
- net EN_R: now also U8.8 (IO15)
- net FET_SW: now also R5.1
- net GND: now also TP11.1, TP13.1, C1.1, C10.2, C11.2, C12.2, C14.2, C15.2, C16.2, C17.2, C18.2, C19.2, C20.2, C22.2, C23.2, C28.1, C29.2, C30.2, C31.1, C6.2, C7.2, C9.2, D11.1 (K), D5.1 (K), J4.A1 (GND), J4.A12 (GND), J4.B1 (GND), J4.B12 (GND), R14.1, R38.2, R39.2, R7.1, R8.1, SW6.1, U5.3 (GND), U5.4 (AGND), U8.1 (GND), U8.40 (GND), U8.41 (GND), U9.2 (V_{SS}); no longer D8.1 (K), D9.1 (K)
- net INT_IMU: now also U8.32 (IO39)
- net PH_L: now also U8.11 (IO18)
- net PH_R: now also U8.9 (IO16)
- net POL_L: now also U8.30 (IO37)
- net POL_M: now also U8.20 (IO12)
- net POL_R: now also U8.19 (IO11)
- net QRE_L: now also U8.21 (IO13)
- net QRE_R: now also U8.25 (IO48)
- net SCL: now also R36.1, TP5.1, U8.28 (IO35), U9.1 (SCL)
- net SDA: now also R40.1, TP7.1, U8.29 (IO36), U9.3 (SDA)
- net SHLD: now also C8.2, R6.2, J4.S1 (SHIELD)
- net USB_VBUS: now also R34.1, J4.A4 (VBUS), J4.A9 (VBUS), J4.B4 (VBUS), J4.B9 (VBUS), TP8.1
- net VBATT: now also R1.2
- net IO21: now reaches D9.2 (A)
- net IO21: now also U8.23 (IO21)
- net IO14: now reaches D8.2 (A)
- net IO14: now also U8.22 (IO14)
- net at U6.1: now also R15.2; no longer R16.2
- net at U6.3: now also R16.2; no longer R15.2
- net at D6.2 (A): now also R33.2
- net at R9.1: now also J4.B5 (CC2)
- net at R10.2: now also J4.A5 (CC1)
- net at J7.2 (Pin_2): now also R18.2
- net VOUT: now reaches D1.2 (A)
- net VOUT: now also C17.1, C20.1, TP12.1
- net at L2.1: now also U5.2 (SW)
- net at BZ1.1 (+): now also R28.1
- net at R35.2: now also D11.2 (A)
- net BTN_IO05 renamed SW1
- net SW1: now also R29.1, U8.6 (IO6)
- net MOTOR_L_1 renamed MOTOR_L1
- net MOTOR_L_2 renamed MOTOR_L2
- net MOTOR_R_1 renamed MOTOR_R1
- net MOTOR_R_2 renamed MOTOR_R2
- net OUT_L_A renamed OUT_LA
- net OUT_LA: now also U8.35 (IO42)
- net OUT_L_B renamed OUT_LB
- net OUT_LB: now also U8.34 (IO41)
- net OUT_R_A renamed OUT_RA
- net OUT_RA: now also U8.5 (IO5)
- net OUT_R_B renamed OUT_RB
- net OUT_RB: now also U8.4 (IO4)
- net PMODE_1: no longer names the net of U2.16 (PMODE)
- net PMODE_1: now also JP1.1 (A), R7.2
- net PMODE_2: no longer names the net of U3.16 (PMODE)
- net PMODE_2: now also JP2.1 (A), R8.2
- net QRE_BACK renamed QRE_B
- net QRE_B: now also R17.1, U8.39 (IO1); no longer R27.2
- net SW: no longer names the net of C13.1, L1.1, U4.2 (SW)
- net VBATT_SHUNT renamed VSHUNT
- net VSHUNT: now also R1.1, R5.2, TP10.1
- removed net VBUS_USB: R34.1, TP13.1
- net VOLTAGE_ALERT renamed ~{V_ALRT}
- net ~{V_ALRT}: now also D3.1 (K), R3.1, U8.12 (IO8)
- net nFAULT renamed ~{D_FLT}
- net ~{D_FLT}: now also U8.17 (IO9); no longer TP11.1
- new net: D8.1 (K), R37.1
- new net: D10.1 (K), R39.1
- new net: D5.2 (A), R32.2
- new net: R13.1, R14.2, U5.6 (FB)
- new net: D9.1 (K), R38.1
- new net: D3.2 (A), R4.2
- new net BZR: R28.2, U8.31 (IO38)
- new net IO47: D10.2 (A), U8.24 (IO47)
- new net IR_MDL: J13.3 (Pin_3), R35.1, U8.38 (IO2)
- new net SHRP_L: U8.18 (IO10)
- new net SHRP_R: U8.33 (IO40)
- new net SW2: R30.1, SW6.2, U8.7 (IO7)
- no-connect marks 16 -> 11
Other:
- note added: "1. Bigger inductor for 3.3V 2. 3. 4. 5. 6. 7."
- note added: "BNO055: 0x28 EEPROM: 0x50 FUSB302 0x25 BQ2589: 0x6A GNSS: 0x3A"
- note added: "BUTTONS"
- note added: "CHANGES:"
- note added: "DISTANCE MEAS."
- note added: "DRBUG and MOUNTING"
- note added: "DRV8874 - Motor driver, H-Bridge Recommended Operating Conditions VM = 4.5V - 37V VIN = 0V - 5v fPWM = 0Hz - 100kHz Vref = 0V - 3.6V"
- note added: "ESP32-S3-WROOM1"
- note added: "I2C ADDR."
- note added: "MISC"
- note added: "MOTOR DRIVING"
- note added: "MOUNT."
- note added: "Memory: 128kbit Vin: 1.6-5.5V Access time: 450ns Max supply curr.: 1mA"
- note added: "RESET"
- note added: "SENSORS"
- note added: "STEP-DOWN CONVERTER 3.3V"
- note added: "STEP-DOWN CONVERTER 5V"
- note added: "TPS565242DRLR Step down converter Input: 3-16V Output: 600mV - 7V Current output: 5A Switching freq.: 600kHz Inductor Inductance: 1.5uH Max. current: 4.7A"
- note removed: "BAD PINOUT"
- note removed: "Battery power"
- note removed: "Buttons for BOOT and ENABLE functions. If the device does not support the auto download mode, you need to get into the download mode manually. To do so, press and hold the BOOT button and then press the RESET button once. After that release the BOOT button."
- note removed: "CONNECTORS and MISC"
- note removed: "CONTROL MODES: PMODE HIGH = PWM PMODE LOW = PH/EN"
- note removed: "CURRENT READING - 2"
- note removed: "DEBUG and MECHANICS"
- note removed: "DISTANCE MEASURING"
- note removed: "DRV8874 - Motor driver, H-Bridge Recommended Operating Conditions VM = 4.5V - 37V VM VIN = 0V - 5v I/PMODE, nSlEEP, EN/IN1, PH/IN2 fPWM = 0Hz - 100kHz EN/IN1, PH/IN2 Vref = 0V - 3.6V VREF Block Diagram:"
- note removed: "EN=reset, BOOT=bootloader mode Enable (EN) is the 3.3V regulator's enable pin. It's pulled up, so connect to ground to disable the 3.3V regulator. This means that you can use this pin connected to a pushbutton to restart your ESP32, for example."
- note removed: "ENABLE RESET"
- note removed: "ESD PROTECTION"
- note removed: "ESP32-S3-WROOM1-N4"
- note removed: "GPIO USB 20 D+ (green) 19 D- (white) GND GND (black) VBUS +5V (red)"
- note removed: "GPIO0 has an internal pullup resistor, so if it is left unconnected then it will pull high."
- note removed: "GPIO0, GPIO45, and GPIO46 are connected to the chip's internal weak pull-up/pull-down resistors at chip reset. These resistors determine the default bit values of the strapping pins. Also, these resistors determine the bit values if the strapping pins are connected to an external high-impedance circuit."
- note removed: "I2C adress = 0x44, 1000100"
- note removed: "MIRRORED"
- note removed: "MOUNTING"
- note removed: "Memory: 128kbit Ma freq.: 1MHz Vin: 1.6-5.5V Access time: 450ns Max supply curr.: 1mA"
- note removed: "NO POL_L CONNECTED FIX TO IO35 NO ENCODERS CONNECTED FIX TO 4 AVAILABLE PINS"
- note removed: "PUSH BUTTONS"
- note removed: "SOME PINS ARE NOT CONNECTED IN SCHEMATIC"
- note removed: "STEPDOWN CONVERTER 3.3V"
- note removed: "STEPDOWN CONVERTER 5V"
- note removed: "SWITCHING SIMULATION - FALSTAD"
- note removed: "Status LED1"
- note removed: "Status LED2"
- note removed: "Status LED3"
- note removed: "Status LED4"
- note removed: "TPS62133 Step down converter Input: 3-17V Output: 5V Current output: 3A Switching freq.: 2.5MHz Inductor Inductance: 2.2uH Max. current: 4.7A"
- note removed: "USB"
- note removed: "USB CONNECTOR"
- note removed: "USB Type-C Connector Data transfer USB connector connected to ESP32 using CDC method"
- note removed: "VBUS Power"
- moved on the sheet: BZ1, C13, C2, C21, C24, C25, C26, C27, C3, C4, C5, C8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

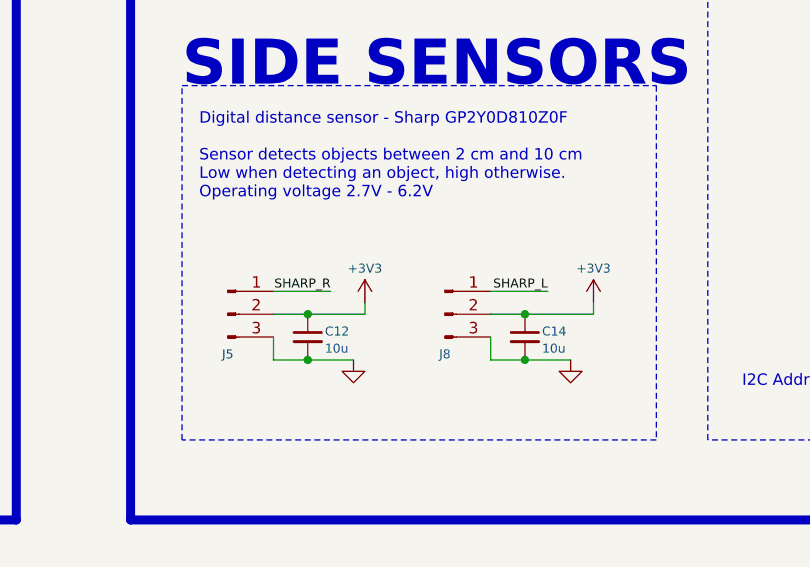
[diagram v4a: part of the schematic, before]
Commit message: silkscreen update and PCB plot
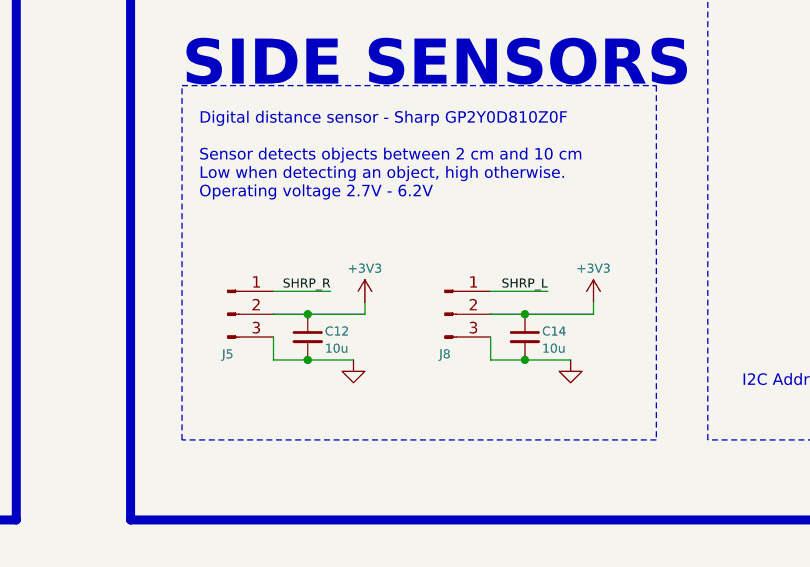
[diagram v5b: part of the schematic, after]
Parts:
- U1: footprint Package_SO:VSSOP-10_3x3mm_P0.5mm -> Package_SO:HVSSOP-10-1EP_3x3mm_P0.5mm_EP1.83x1.89mm
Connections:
- net SHARP_L is gone; now on net SHRP_L: J8.1 (Pin_1)
- net SHARP_R is gone; now on net SHRP_R: J5.1 (Pin_1)
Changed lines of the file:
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@@
 		)
 	)
-	(label "SHARP_R"
+	(label "SHRP_R"
 		(at 214.63 326.39 180)
 		(effects
@@
 		)
 	)
-	(label "SHARP_L"
+	(label "SHRP_L"
 		(at 238.76 326.39 180)
 		(effects
@@
 			)
 		)
-		(property "Footprint" "Package_SO:VSSOP-10_3x3mm_P0.5mm"
+		(property "Footprint" "Package_SO:HVSSOP-10-1EP_3x3mm_P0.5mm_EP1.83x1.89mm"
 			(at 119.38 162.56 0)
 			(hide yes)

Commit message: new MK5.5 update
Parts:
- removed TP3: TestPoint, TestPoint:TestPoint_Pad_D1.5mm, symbol Connector:TestPoint
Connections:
- net GND: now also TP9.1
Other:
- moved on the sheet: TP11, TP13, TP5, TP7, TP9
